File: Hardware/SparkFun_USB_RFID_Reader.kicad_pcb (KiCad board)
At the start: 4 copper layers, 44.5 x 31.8 mm, 52 parts, among them J1 USB_C_Receptacle, J2 Conn_01x07_2.0mm, J3 Conn_01x05_2.0mm, J5 Conn_01x08, Q1 MMBT2222A, U3 CH340C

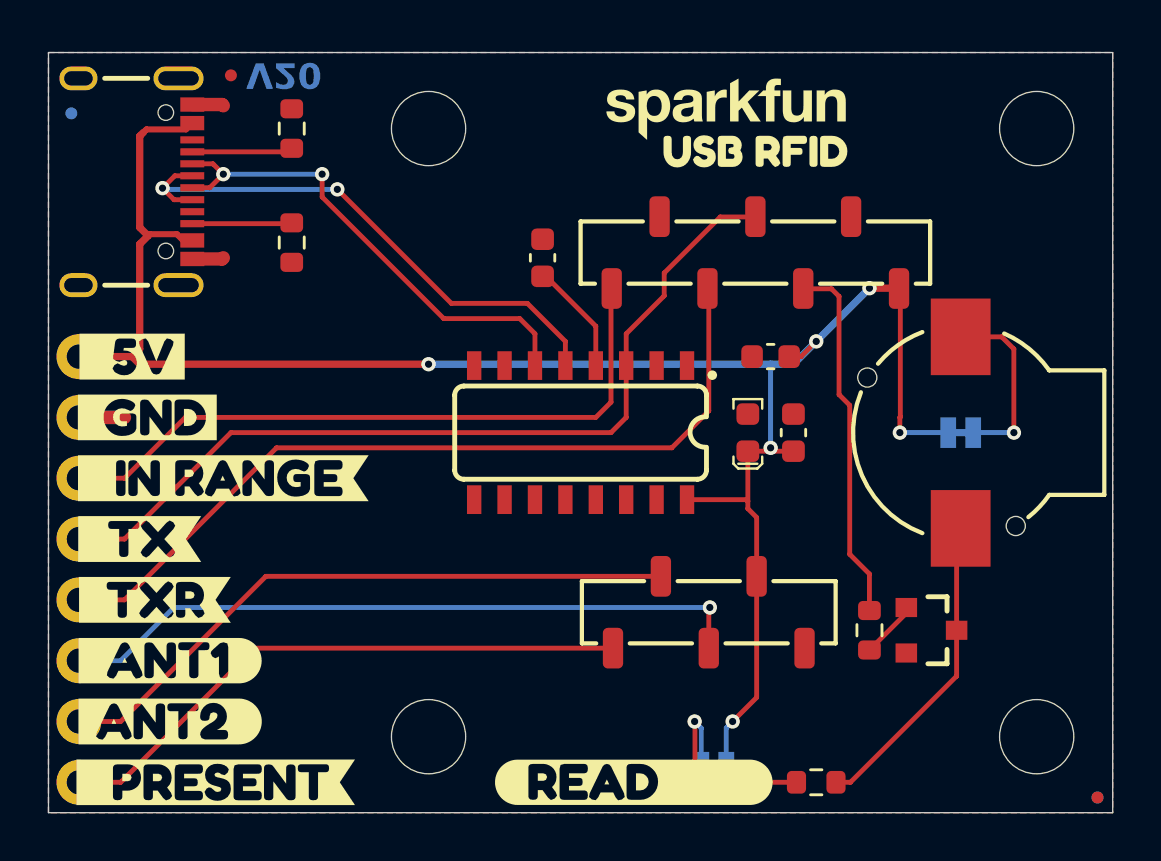
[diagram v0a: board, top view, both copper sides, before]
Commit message: Center USB-C Connector
- Move USB-C connector to center
- Arrange 0.1" headers to either side
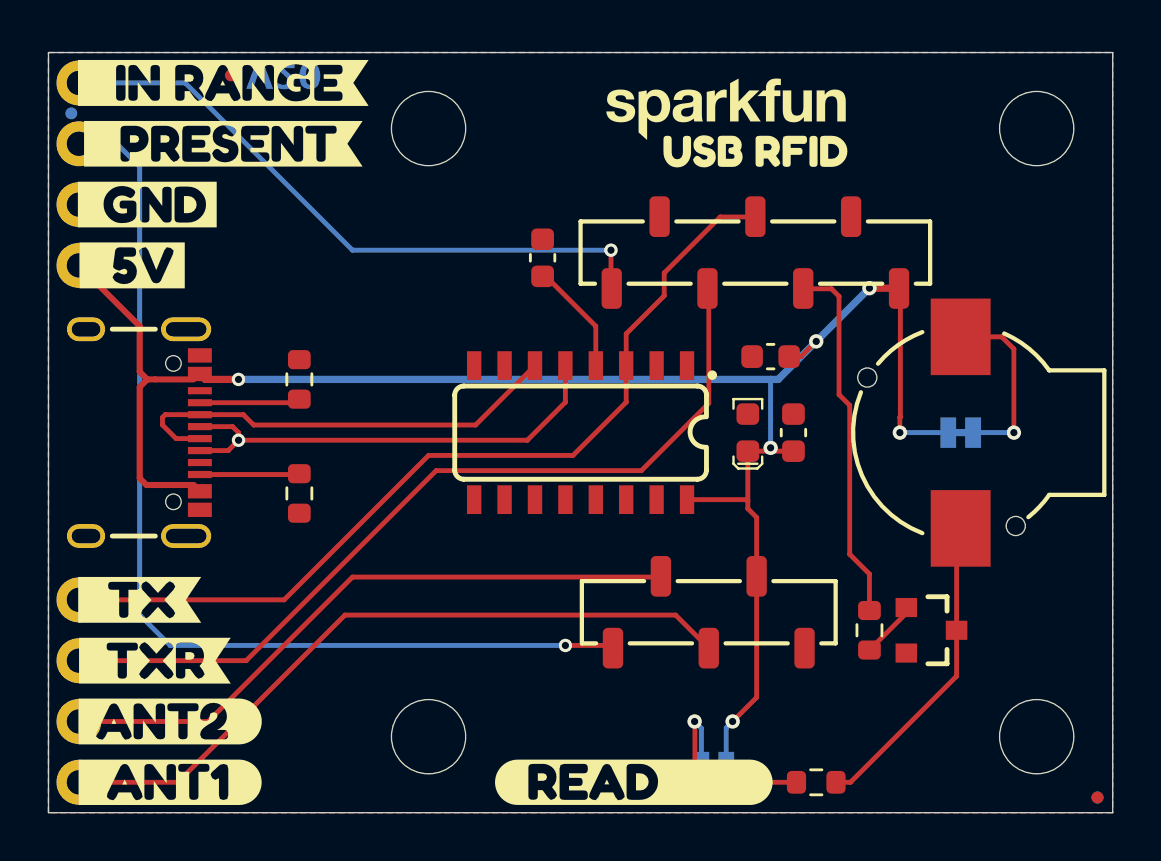
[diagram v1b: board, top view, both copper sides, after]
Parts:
- removed J5: Conn_01x08, SparkFun-Connector:1x08
- removed kibuzzard-677EF197: G***, kibuzzard-677EF197
- added J4: Conn_01x04, SparkFun-Connector:1x04, F.Cu at (124.8, 111.8)
- added J6: Conn_01x04, SparkFun-Connector:1x04, F.Cu at (124.8, 82.6)
- added kibuzzard-678FF5A6: G***, kibuzzard-678FF5A6, B.Cu at (146.7, 99.1)
- moved kibuzzard-677EEBF5 26.7 mm to (130.8, 85.1)
- moved kibuzzard-677EF067 26.7 mm to (130.8, 85.1)
- moved kibuzzard-677EEB0A 16.5 mm to (130.8, 82.5)
- moved kibuzzard-677EF080 16.5 mm to (130.8, 82.5)
- moved J1 10.5 mm to (130.2, 97.2)
- moved R1 10.5 mm to (134.0, 94.9)
- moved R2 10.5 mm to (134.0, 99.7)
- moved kibuzzard-677EEF6B 8.90 mm to (127.6, 87.6)
- moved kibuzzard-677EEB4C 8.89 mm to (127.6, 87.6)
- moved kibuzzard-677EF000 5.09 mm to (128.6, 111.8)
- moved kibuzzard-677EEB9B 5.08 mm to (128.6, 111.8)
- moved kibuzzard-677EEA49 3.81 mm to (127.0, 90.2)
- moved kibuzzard-677EEF34 3.81 mm to (127.0, 90.2)
- moved kibuzzard-677EEFDD 2.56 mm to (128.0, 106.7)
- moved kibuzzard-677EF074 2.56 mm to (127.3, 104.1)
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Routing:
- net CARD_PRESENT: track 24.6 -> 42.0 mm, vias 0 -> 1
- net GND: track 6.13 -> 0.00 mm
- net 5V: track 81.2 -> 76.5 mm
- net Net-(U3-UD+): track 23.4 -> 19.7 mm, vias 2 -> 1
- net Net-(U3-UD-): track 20.7 -> 18.9 mm, vias 2 -> 0
- net TAG_IN_RANGE: track 28.3 -> 26.7 mm, vias 0 -> 1
- net DATA1: track 34.7 -> 35.6 mm
- net ANT1: track 29.0 -> 29.8 mm, vias 1 -> 0
- net DATA0: track 36.5 -> 37.2 mm

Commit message: Move fiducial from silk. Add version in copper. Move OSHW gear from silk.
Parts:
- removed kibuzzard-677EF466: G***, kibuzzard-677EF466
- removed kibuzzard-678FF5A6: G***, kibuzzard-678FF5A6
- added kibuzzard-67901575: G***, kibuzzard-67901575, B.Cu at (146.7, 99.1)
- added kibuzzard-6790157C: G***, kibuzzard-6790157C, F.Cu at (153.0, 85.7)
- moved Ref** 41.6 mm to (161.0, 109.2)
- moved FID2 6.36 mm to (137.5, 82.5)
- moved G*** 1.27 mm to (153.0, 83.5)
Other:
- board text added: "v20"

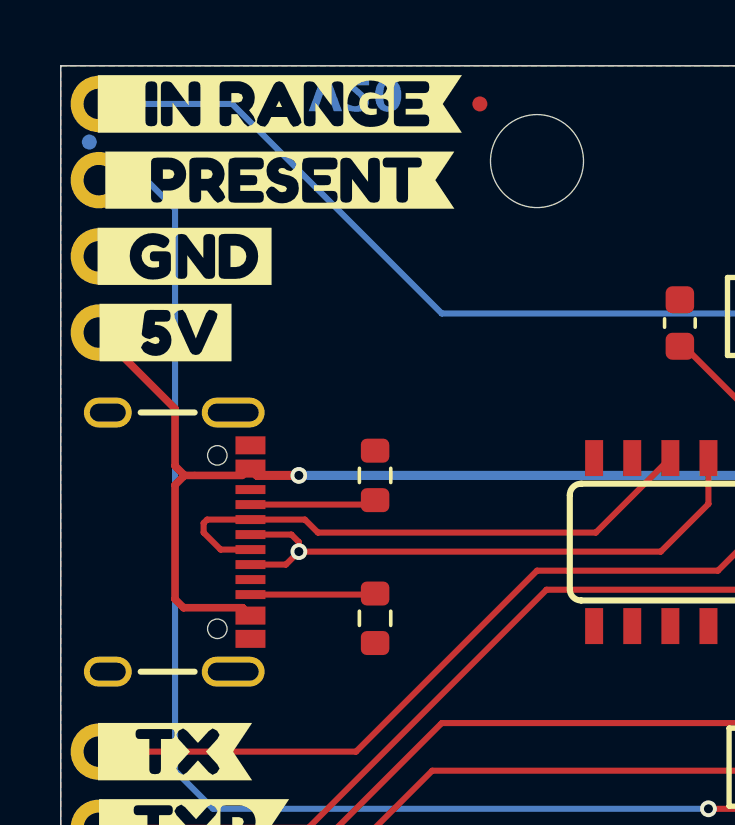
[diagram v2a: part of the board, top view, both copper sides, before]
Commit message: Reduce to two layer board
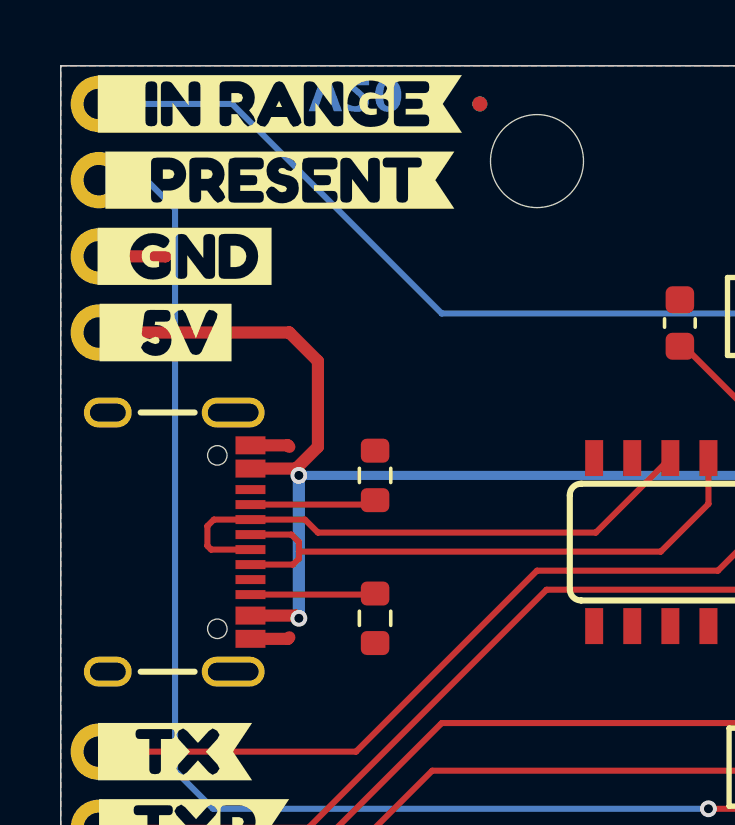
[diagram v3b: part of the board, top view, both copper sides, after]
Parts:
- moved FID3 13.1 mm to (137.5, 82.5)
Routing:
- net GND: track 0.00 -> 4.86 mm
- net 5V: track 76.5 -> 79.8 mm, vias 6 -> 7
- net Net-(U3-UD+): track 19.7 -> 19.8 mm, vias 1 -> 0
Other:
- copper layers 4 -> 2

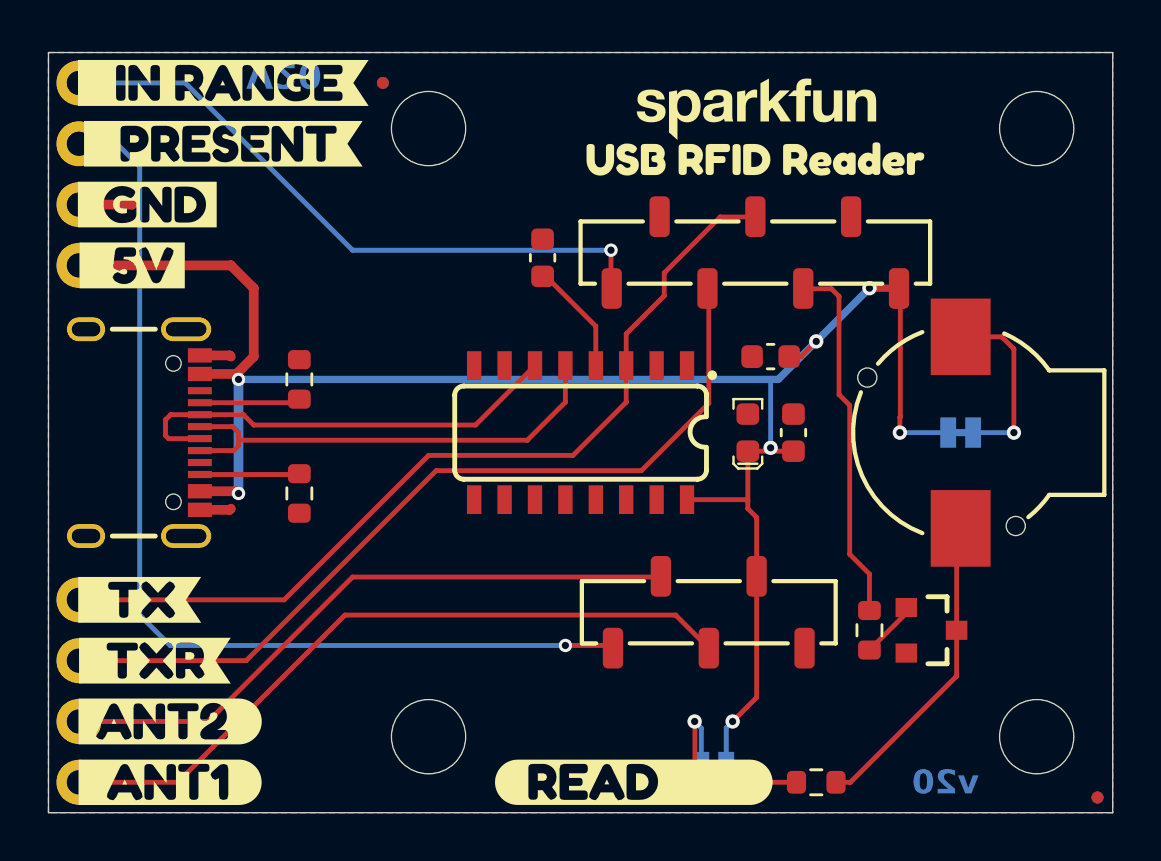
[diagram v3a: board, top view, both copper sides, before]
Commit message: Align silk labels
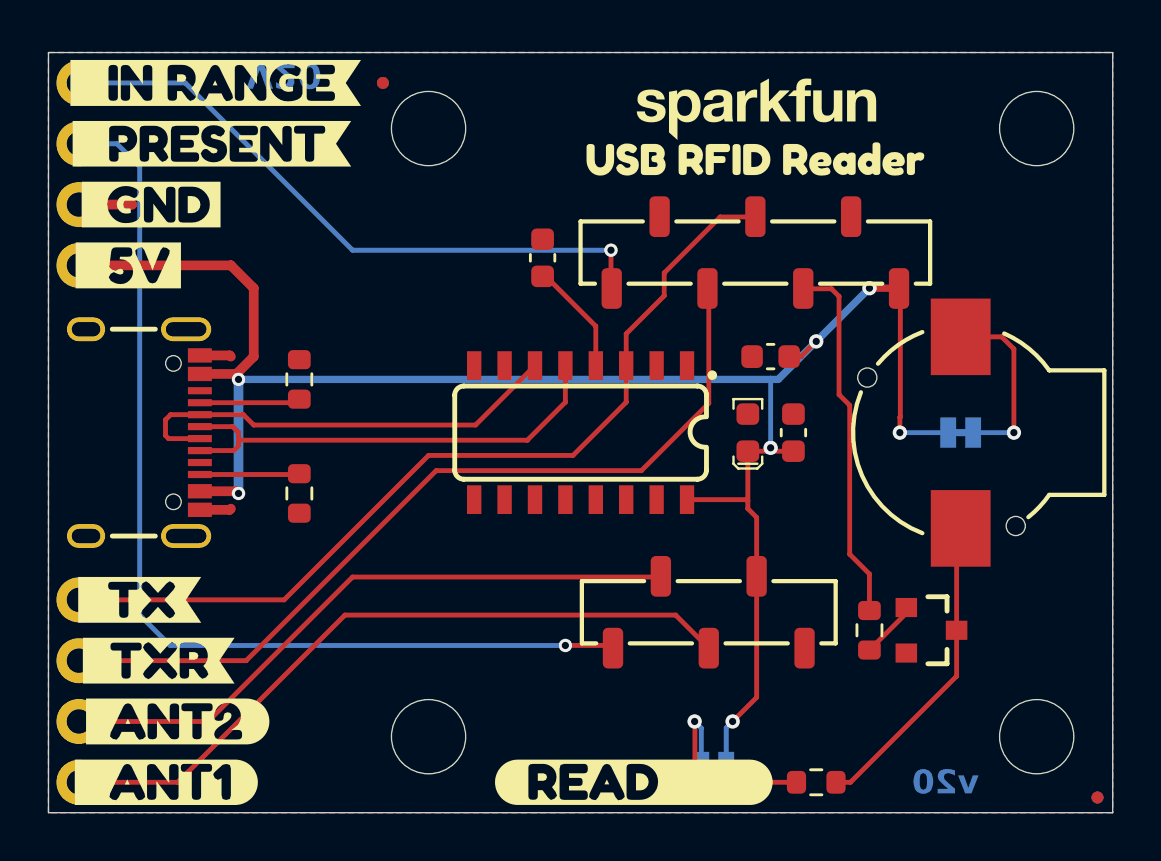
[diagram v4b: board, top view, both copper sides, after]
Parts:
- removed kibuzzard-677EEB9B: G***, kibuzzard-677EEB9B
- removed kibuzzard-677EEBA7: G***, kibuzzard-677EEBA7
- added kibuzzard-67901A90: G***, kibuzzard-67901A90, F.Cu at (128.9, 109.2)
- added kibuzzard-67901A9C: G***, kibuzzard-67901A9C, F.Cu at (128.4, 111.8)
- moved kibuzzard-677EEBF5 0.48 mm to (130.3, 85.1)
- moved kibuzzard-677EEB0A 0.32 mm to (130.5, 82.5)
- moved kibuzzard-677EF00A 0.32 mm to (128.9, 109.2)
- moved kibuzzard-677EF067 0.32 mm to (130.5, 85.1)
- moved kibuzzard-677EF080 0.32 mm to (130.5, 82.5)
- moved kibuzzard-677EEB6C 0.16 mm to (128.1, 106.7)
- moved kibuzzard-677EEA49 0.16 mm to (126.8, 90.2)
- moved kibuzzard-677EEB4C 0.16 mm to (127.8, 87.6)
- moved kibuzzard-677EEF34 0.16 mm to (126.8, 90.2)
- moved kibuzzard-677EEF6B 0.16 mm to (127.8, 87.6)

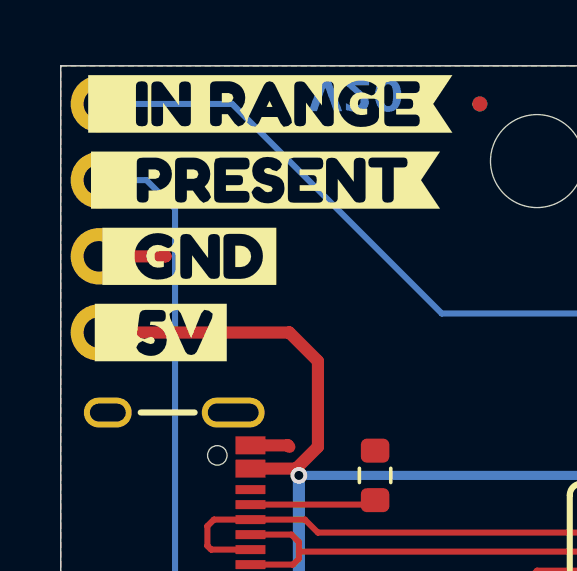
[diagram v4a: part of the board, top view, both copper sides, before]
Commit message: Fix DRC error
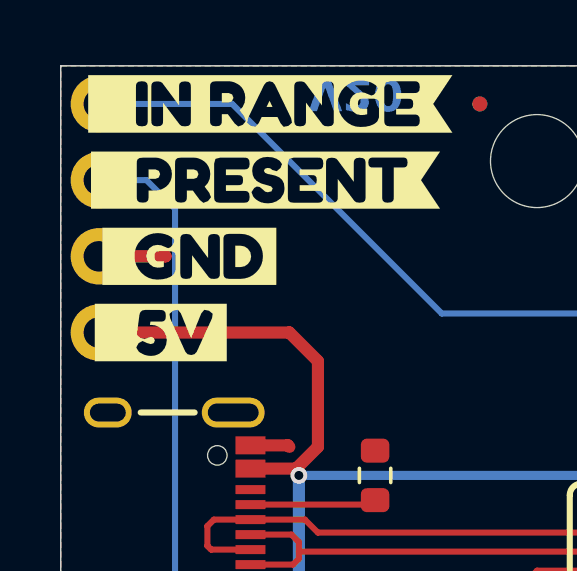
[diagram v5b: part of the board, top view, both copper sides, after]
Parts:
- C3: value 470nF -> 0.1uF
- R3: value 4.7k -> 1k
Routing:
- net GND: track 4.86 -> 6.76 mm
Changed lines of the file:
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@@
 				(font
 					(size 0.001 0.001)
+					(thickness 0.15)
 				)
 			)
@@
 				(font
 					(size 0.001 0.001)
+					(thickness 0.15)
 				)
 			)
@@
 				(font
 					(size 0.001 0.001)
+					(thickness 0.15)
 				)
 			)
@@
 				(font
 					(size 0.001 0.001)
+					(thickness 0.15)
 				)
 			)
@@
 			)
 		)
-		(property "Value" "470nF"
+		(property "Value" "0.1uF"
 			(at 0 1.43 -90)
 			(layer "F.Fab")
@@
 			)
 		)
-		(property "PROD_ID" "CAP-13216"
+		(property "PROD_ID" "CAP-00810"
 			(at 0 0 90)
 			(unlocked yes)
@@
 			)
 		)
-		(property "Voltage" "10V"
+		(property "Voltage" "25V"
 			(at 0 0 90)
 			(unlocked yes)
@@
 			)
 		)
-		(property "Tolerance" "10%"
+		(property "Tolerance" "20%"
 			(at 0 0 90)
 			(unlocked yes)
@@
 			)
 		)
-		(property "Value" "4.7k"
+		(property "Value" "1k"
 			(at 0 1.43 0)
 			(layer "F.Fab")
@@
 			)
 		)
-		(property "PROD_ID" "RES-07857"
+		(property "PROD_ID" "RES-07856"
 			(at 0 0 180)
 			(unlocked yes)
@@
 		(fp_arc
 			(start 1.5653 -5.257777)
-			(mid 1.834725 -5.146217)
+			(mid 1.834722 -5.146216)
 			(end 1.9463 -4.8768)
 			(stroke
@@
 		(net 34)
 	)
+	(segment
+		(start 126.682499 87.630001)
+		(end 126.6825 87.63)
+		(width 0.4064)
+		(layer "B.Cu")
+		(net 34)
+	)
+	(segment
+		(start 124.7775 87.630001)
+		(end 126.682499 87.630001)
+		(width 0.4064)
+		(layer "B.Cu")
+		(net 34)
+	)

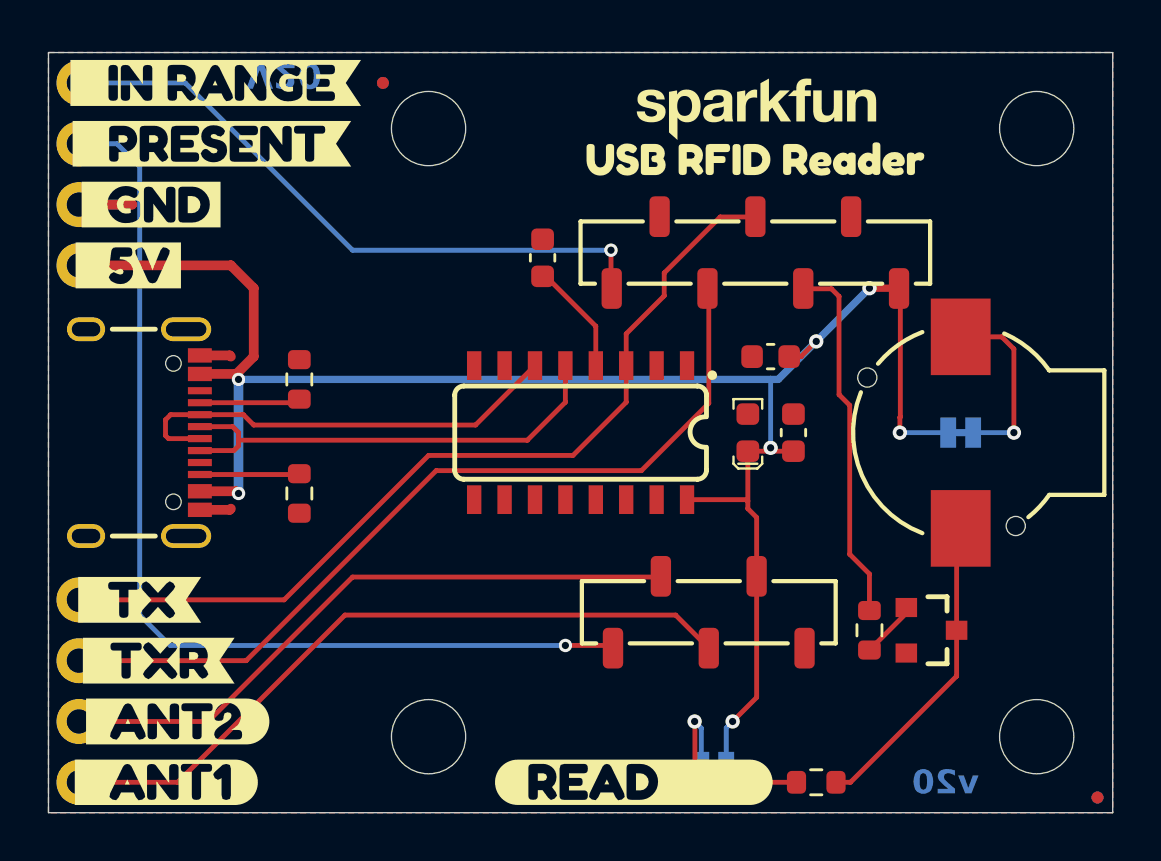
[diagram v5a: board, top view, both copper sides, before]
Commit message: Change to PTH connectors
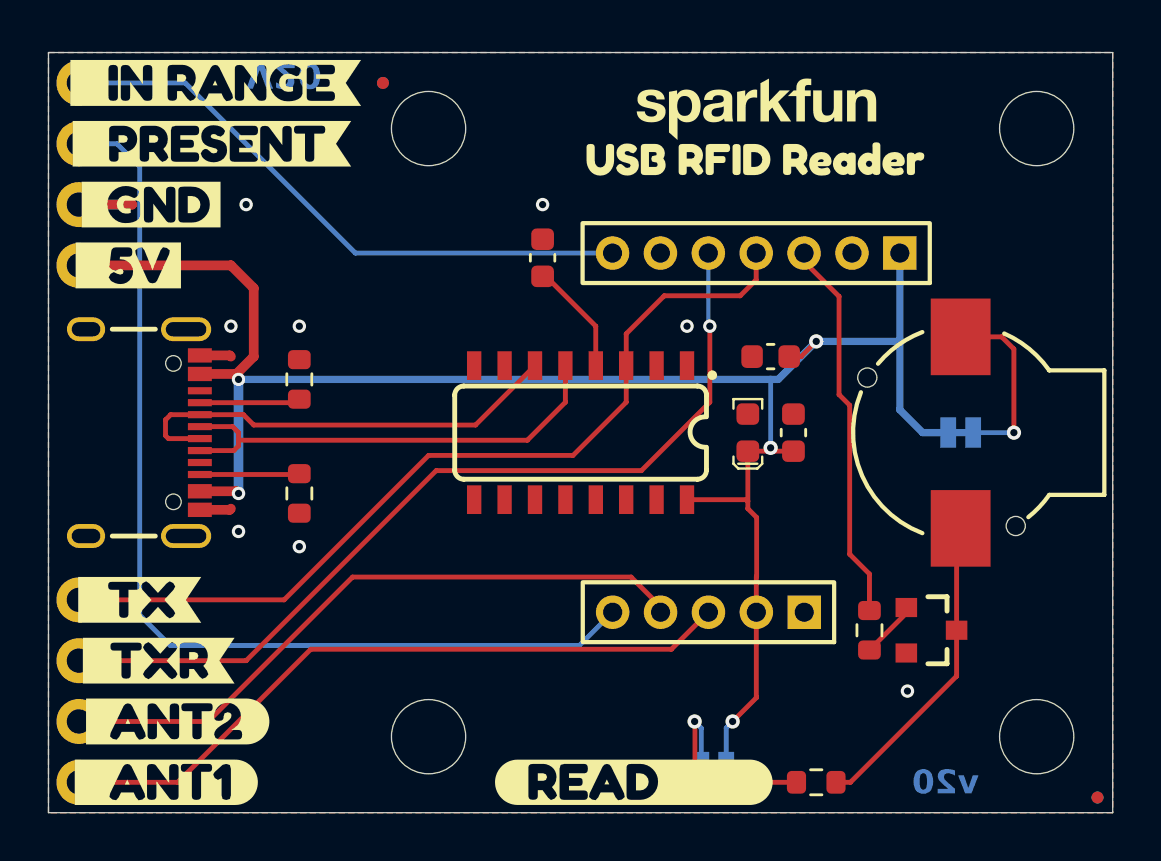
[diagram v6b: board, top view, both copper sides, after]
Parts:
- J2: footprint SparkFun-Connector:1x07_2.0mm_SMD_Pin1RightDown -> SparkFun-Connector:1x07_2.0mm
- J3: footprint SparkFun-Connector:1x05_2.0mm_SMD_Pin1RightDown -> SparkFun-Connector:1x05_2.0mm
- moved J2 6.03 mm to (159.1, 89.7), turned to 180 degrees
- moved J3 3.99 mm to (155.1, 104.7), turned to 180 degrees
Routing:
- net TAG_IN_RANGE: track 26.7 -> 25.2 mm, vias 1 -> 0
- net DATA1: track 35.6 -> 37.1 mm, vias 0 -> 1
- net LED: track 15.2 -> 16.1 mm
- net DATA0: track 37.2 -> 36.6 mm
- net ANT1: track 29.8 -> 29.2 mm
- net CARD_PRESENT: track 42.0 -> 42.5 mm, vias 1 -> 0
- net 5V: vias 7 -> 5
- net GND: vias 0 -> 8
